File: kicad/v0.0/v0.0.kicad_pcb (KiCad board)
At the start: 2 copper layers, 51 parts, among them J1 USB_B_Micro, J2 9V_IN, J3 LED, J4 MOTOR, Q1 IRF520, SW1 RST, SW2 FLASH, SW3 OPEN/CLOSE, U1 MCP2221AxSL, U2 MAX14872ETC+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

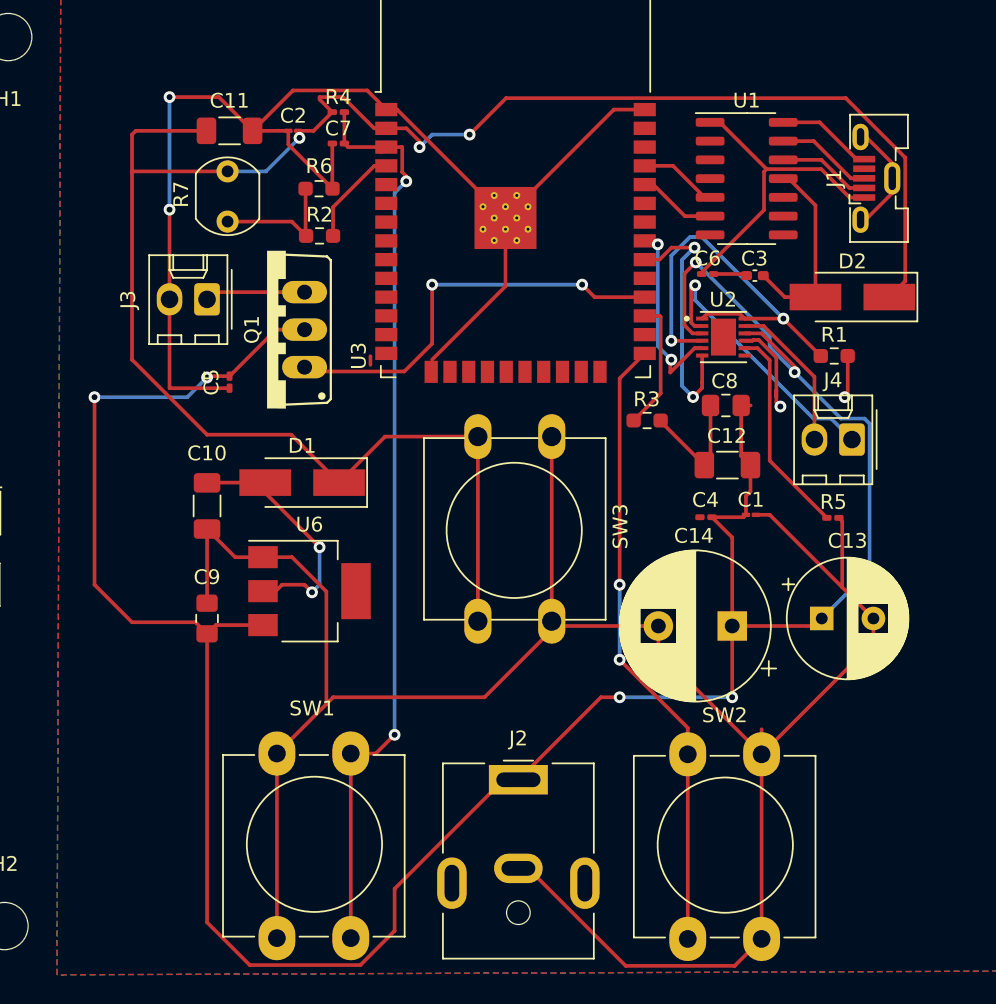
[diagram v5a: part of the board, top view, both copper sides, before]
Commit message: removed ground
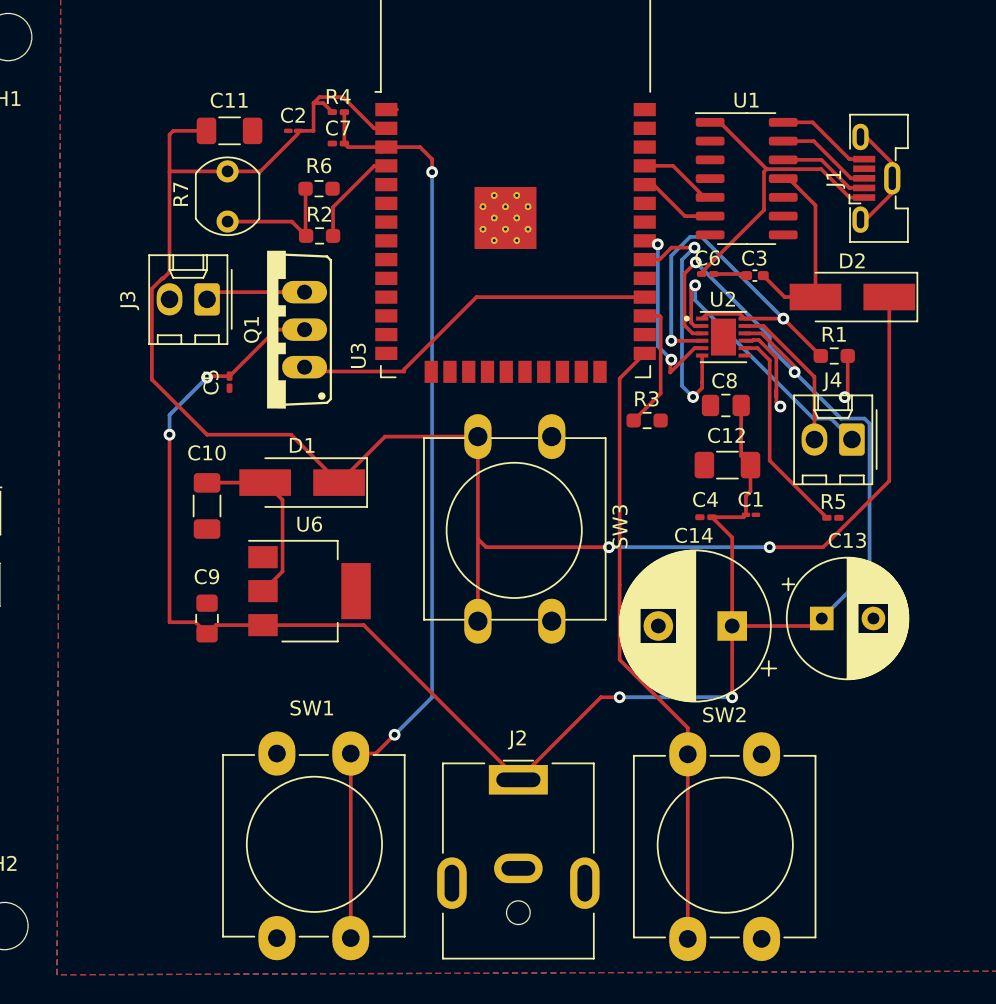
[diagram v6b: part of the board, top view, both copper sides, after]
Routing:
- net GND: track 265.4 -> 20.6 mm, vias 4 -> 2
- net +9V: track 179.3 -> 143.2 mm
- net +3V3: track 133.9 -> 122.1 mm, vias 3 -> 2
- net Net-(D1-Pad2): track 17.4 -> 12.3 mm, vias 2 -> 0
- net /LED: track 28.3 -> 24.9 mm, vias 2 -> 0
- net Net-(C7-Pad1): track 62.9 -> 65.0 mm
- net Net-(SW2-Pad1): vias 2 -> 0

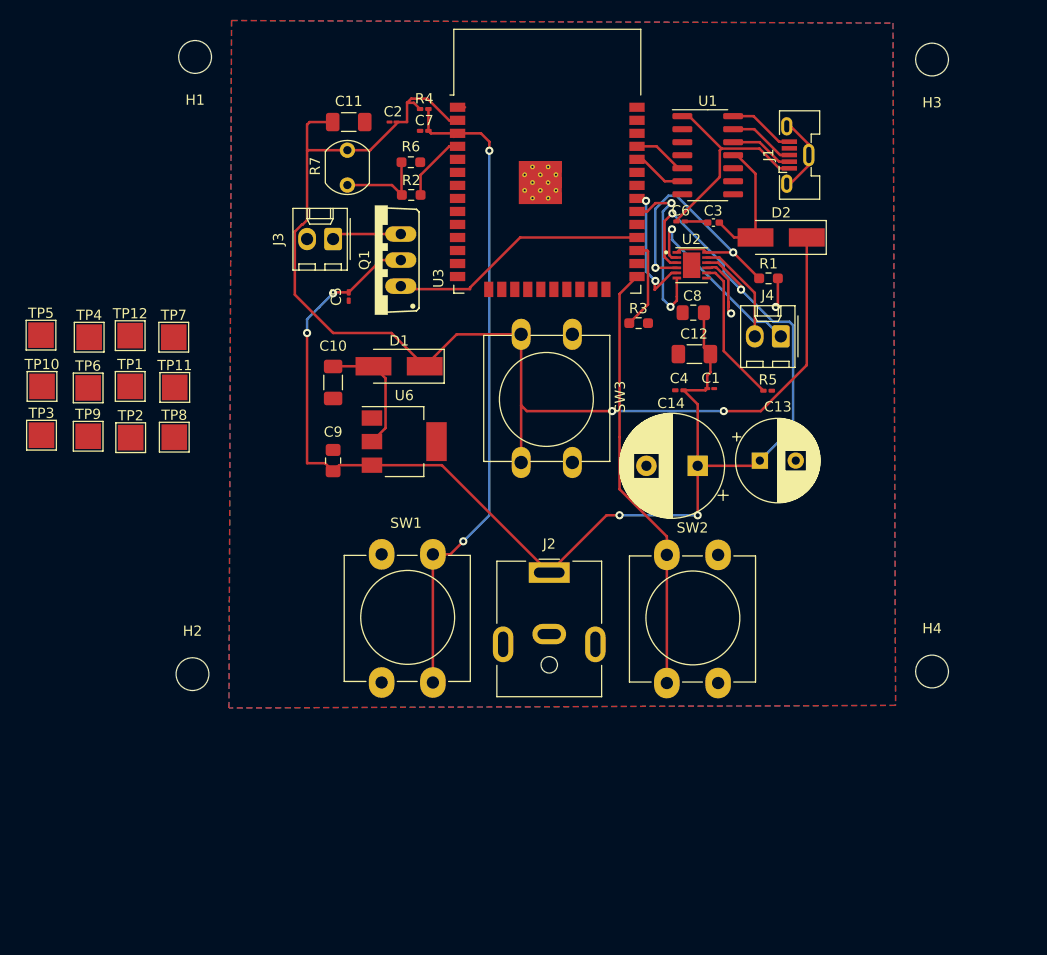
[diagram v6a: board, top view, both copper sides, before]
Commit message: made resistors and capacitors standard size
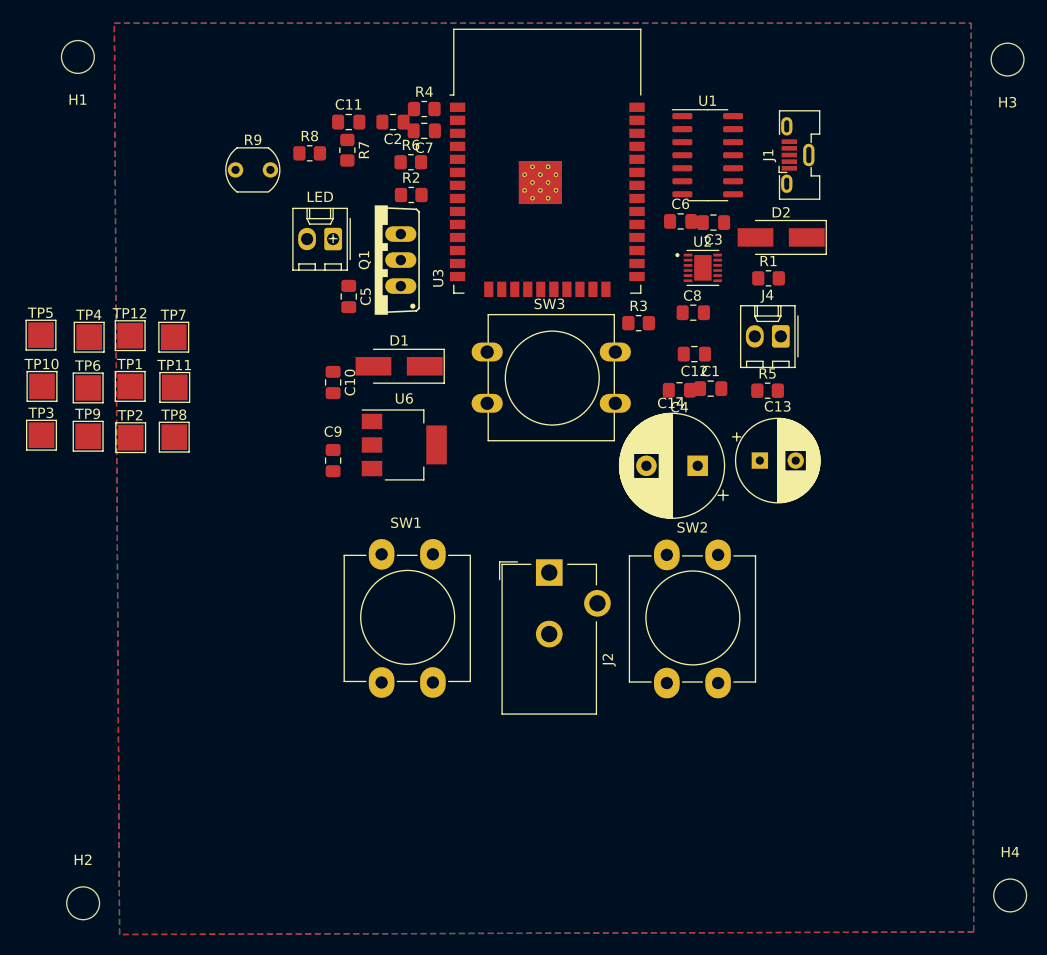
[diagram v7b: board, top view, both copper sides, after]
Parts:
- added R8: 20k, Resistor_SMD:R_0805_2012Metric_Pad1.20x1.40mm_HandSolder, F.Cu at (122.2, 63.8)
- added R9: R_Photo, OptoDevice:R_LDR_5.1x4.3mm_P3.4mm_Vertical, F.Cu at (114.9, 65.4)
- C1, C2: footprint Capacitor_SMD:C_01005_0402Metric_Pad0.57x0.30mm_HandSolder -> Capacitor_SMD:C_0805_2012Metric_Pad1.18x1.45mm_HandSolder
- C10, C11, C12: footprint Capacitor_SMD:C_1206_3216Metric_Pad1.33x1.80mm_HandSolder -> Capacitor_SMD:C_0805_2012Metric_Pad1.18x1.45mm_HandSolder
- C3: footprint Capacitor_SMD:C_0402_1005Metric_Pad0.74x0.62mm_HandSolder -> Capacitor_SMD:C_0805_2012Metric_Pad1.18x1.45mm_HandSolder
- C4, C5, C6, C7: footprint Capacitor_SMD:C_0201_0603Metric_Pad0.64x0.40mm_HandSolder -> Capacitor_SMD:C_0805_2012Metric_Pad1.18x1.45mm_HandSolder
- J2: footprint Connector_BarrelJack:BarrelJack_CUI_PJ-063AH_Horizontal -> Connector_BarrelJack:BarrelJack_CUI_PJ-102AH_Horizontal
- R1, R2, R3: footprint Resistor_SMD:R_0603_1608Metric_Pad0.98x0.95mm_HandSolder -> Resistor_SMD:R_0805_2012Metric_Pad1.20x1.40mm_HandSolder
- R4, R5: value 10k -> 1k; footprint Resistor_SMD:R_0201_0603Metric_Pad0.64x0.40mm_HandSolder -> Resistor_SMD:R_0805_2012Metric_Pad1.20x1.40mm_HandSolder
- R6: value 20k -> 10k; footprint Resistor_SMD:R_0603_1608Metric_Pad0.98x0.95mm_HandSolder -> Resistor_SMD:R_0805_2012Metric_Pad1.20x1.40mm_HandSolder
- R7: value R_Photo -> 10k; footprint OptoDevice:R_LDR_5.1x4.3mm_P3.4mm_Vertical -> Resistor_SMD:R_0805_2012Metric_Pad1.20x1.40mm_HandSolder
- moved H2 24.8 mm to (100.1, 136.9)
- moved H4 23.1 mm to (190.5, 136.1)
- moved H1 11.4 mm to (99.6, 54.4)
- moved SW3 8.49 mm to (139.5, 83.1), turned to 0 degrees
- moved H3 7.37 mm to (190.2, 54.6)
- moved U2 1.13 mm to (160.5, 74.9)
- moved U6 0.33 mm to (131.4, 92.2)
- turned R3 to 0 degrees
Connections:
- C10 pad 1: Net-(D1-Pad2) -> Net-(C10-Pad1)
- D1 pad 2: Net-(D1-Pad2) -> Net-(C10-Pad1)
- Q1 pad S: Net-(J3-Pad1) -> Net-(Q1-PadS)
- R2 pad 1: Net-(R6-Pad1) -> Net-(R2-Pad1)
- R3 pad 1: GND -> Net-(R3-Pad1)
- R4 pad 1: +3V3 -> Net-(R3-Pad1)
- R4 pad 2: Net-(C7-Pad1) -> GND
- R5 pad 1: Net-(R5-Pad1) -> Net-(Q1-PadS)
- R5 pad 2: GND -> Net-(J3-Pad1)
- R6 pad 1: Net-(R6-Pad1) -> +3V3
- R6 pad 2: GND -> Net-(C7-Pad1)
- R7 pad 1: +3V3 -> Net-(R7-Pad1)
- R7 pad 2: Net-(R6-Pad1) -> GND
- SW3 pad 1: GND -> Net-(R3-Pad1)
- TP1 pad 1: unconnected-(TP1-Pad1) -> /LED
- TP2 pad 1: unconnected-(TP2-Pad1) -> /FWD
- TP3 pad 1: unconnected-(TP3-Pad1) -> /REV
- TP4 pad 1: unconnected-(TP4-Pad1) -> +9V
- TP5 pad 1: unconnected-(TP5-Pad1) -> Net-(C10-Pad1)
- TP6 pad 1: unconnected-(TP6-Pad1) -> Net-(C3-Pad1)
- TP7 pad 1: unconnected-(TP7-Pad1) -> Net-(R3-Pad1)
- U2 pad 8: Net-(R5-Pad1) -> Net-(R7-Pad1)
- U6 pad 2: Net-(D1-Pad2) -> Net-(C10-Pad1)
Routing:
- net +9V: track 143.2 -> 0.00 mm, vias 6 -> 0
- net +3V3: track 122.1 -> 0.00 mm, vias 2 -> 0
- net Net-(C7-Pad1): track 65.0 -> 0.00 mm, vias 2 -> 0
- net Net-(SW2-Pad1): track 42.3 -> 0.00 mm
- net /SNS: track 27.6 -> 0.00 mm, vias 2 -> 0
- net /LED: track 24.9 -> 0.00 mm
- net Net-(C6-Pad1): track 21.5 -> 0.00 mm
- net GND: track 20.6 -> 0.00 mm, vias 2 -> 0
- net Net-(J4-Pad1): track 19.1 -> 0.00 mm, vias 1 -> 0
- net /REV: track 17.6 -> 0.00 mm, vias 2 -> 0
- net Net-(R5-Pad1): track 14.3 -> 0.00 mm
- net Net-(C3-Pad1): track 13.3 -> 0.00 mm
- net /FWD: track 12.9 -> 0.00 mm, vias 2 -> 0
- net Net-(D1-Pad2): track 12.3 -> 0.00 mm
- net Net-(J4-Pad2): track 10.4 -> 0.00 mm
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
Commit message: blah
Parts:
- moved TP8 108.5 mm to (24.9, 22.9)
- moved TP11 101.0 mm to (27.2, 27.4)
- moved C13 100.5 mm to (67.3, 75.4)
- moved TP1 99.9 mm to (204.5, 82.8)
- moved TP9 98.9 mm to (29.2, 22.9)
- moved TP10 94.1 mm to (22.9, 27.4)
- moved TP12 91.2 mm to (31.2, 27.4)
- moved U2 91.1 mm to (70.4, 87.9)
- moved R1 85.8 mm to (81.3, 70.4)
- moved C14 84.1 mm to (76.5, 84.6), turned to 0 degrees
- moved C8 83.4 mm to (76.5, 73.2)
- moved C4 82.4 mm to (76.5, 76.5)
- moved Q1 81.9 mm to (210.3, 78.7)
- moved C5 81.9 mm to (207.8, 82.3)
- moved J3 81.9 mm to (206.2, 76.7)
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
